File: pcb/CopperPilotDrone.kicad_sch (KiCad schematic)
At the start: 69 parts, among them IC1 MCP73833T-AMI/UN, J1 USB_C_Receptacle_USB2.0, J2 Conn_01x02_Female, J3 B2B-PH-SM4-TB(LF)(SN), J4 Conn_01x02_Female, J5 Conn_01x02_Female, J6 Conn_01x02_Female, SW1 PCM12SMTR, SW2 TS-1187A, SW3 TS-1187A, T1 SI2302DS-T1, T2 SI2302DS-T1, T3 SI2302DS-T1, T4 SI2302DS-T1, U2 AO3401, U3 AP2112K-3.3TRG1, U8 ESP32-S3-WROOM-1-N8R8, U9 MPU-6500

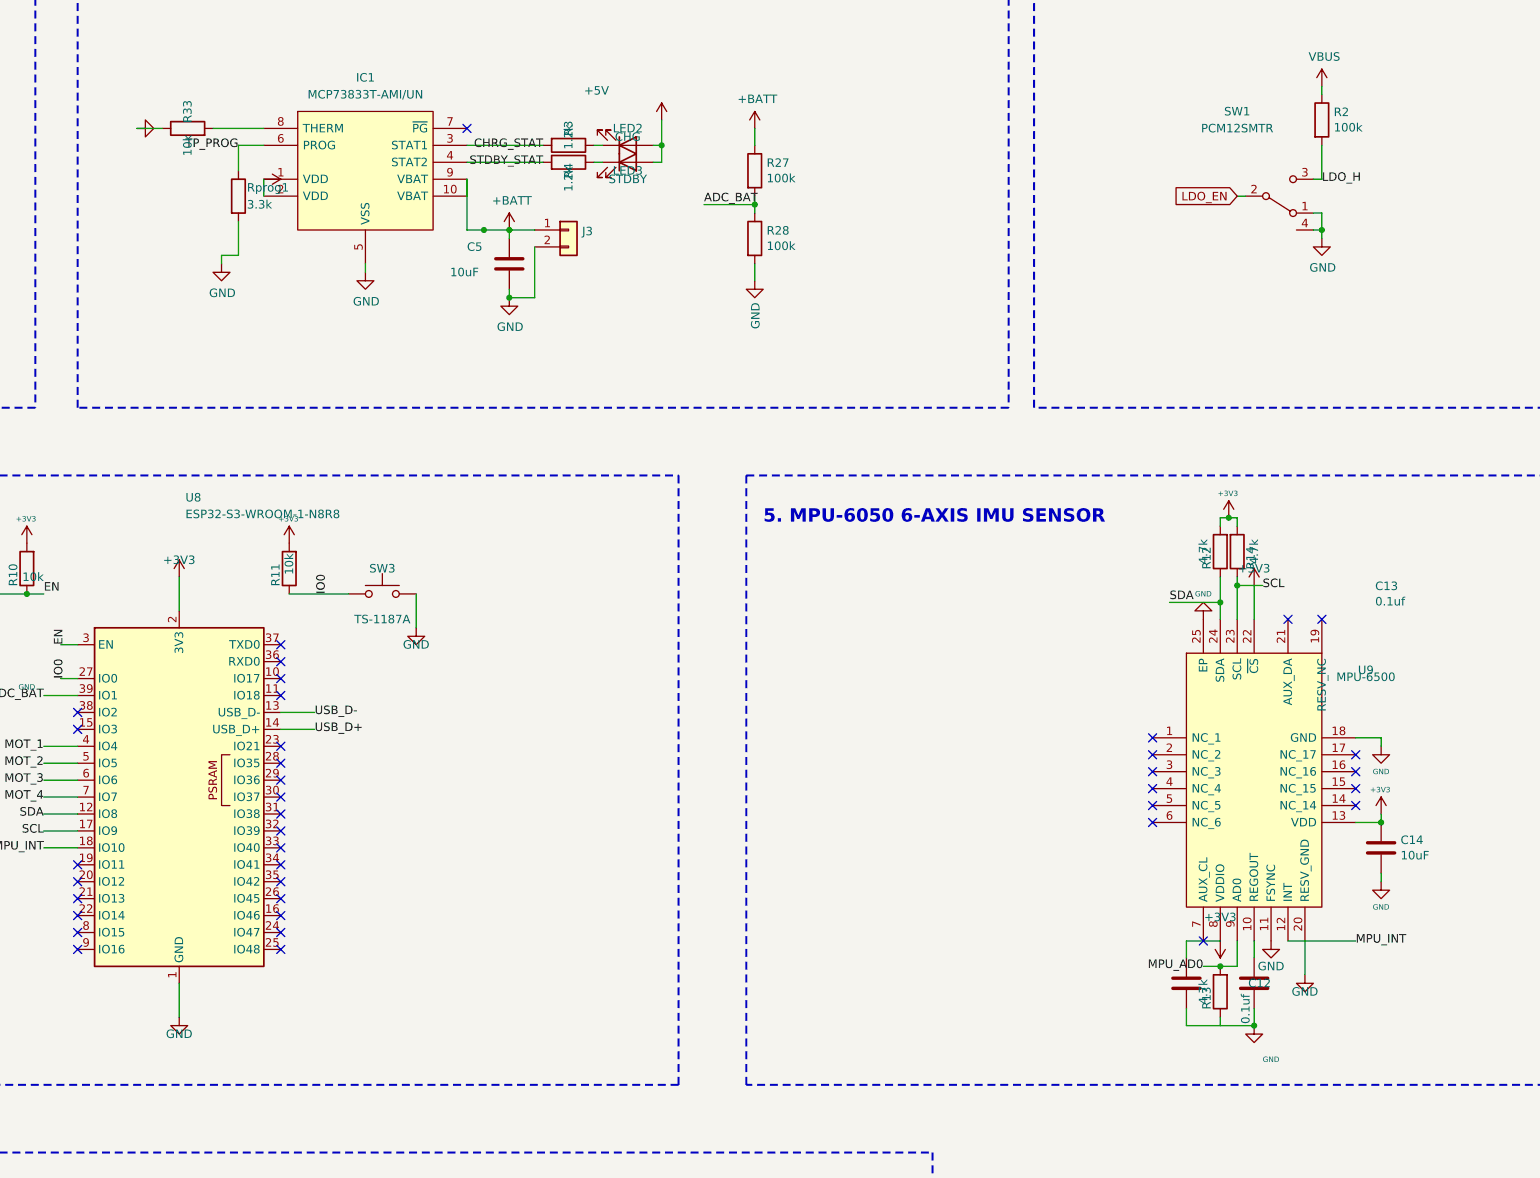
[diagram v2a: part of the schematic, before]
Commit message: fix(sch): complete GND symbol #PWR913 and pin ties on IC1/U9 for zero ERC
Verify 0 ERC violations across all severities via kicad-cli sch erc.

Co-Authored-By: CopperPilot <noreply@copperpilot.ai>
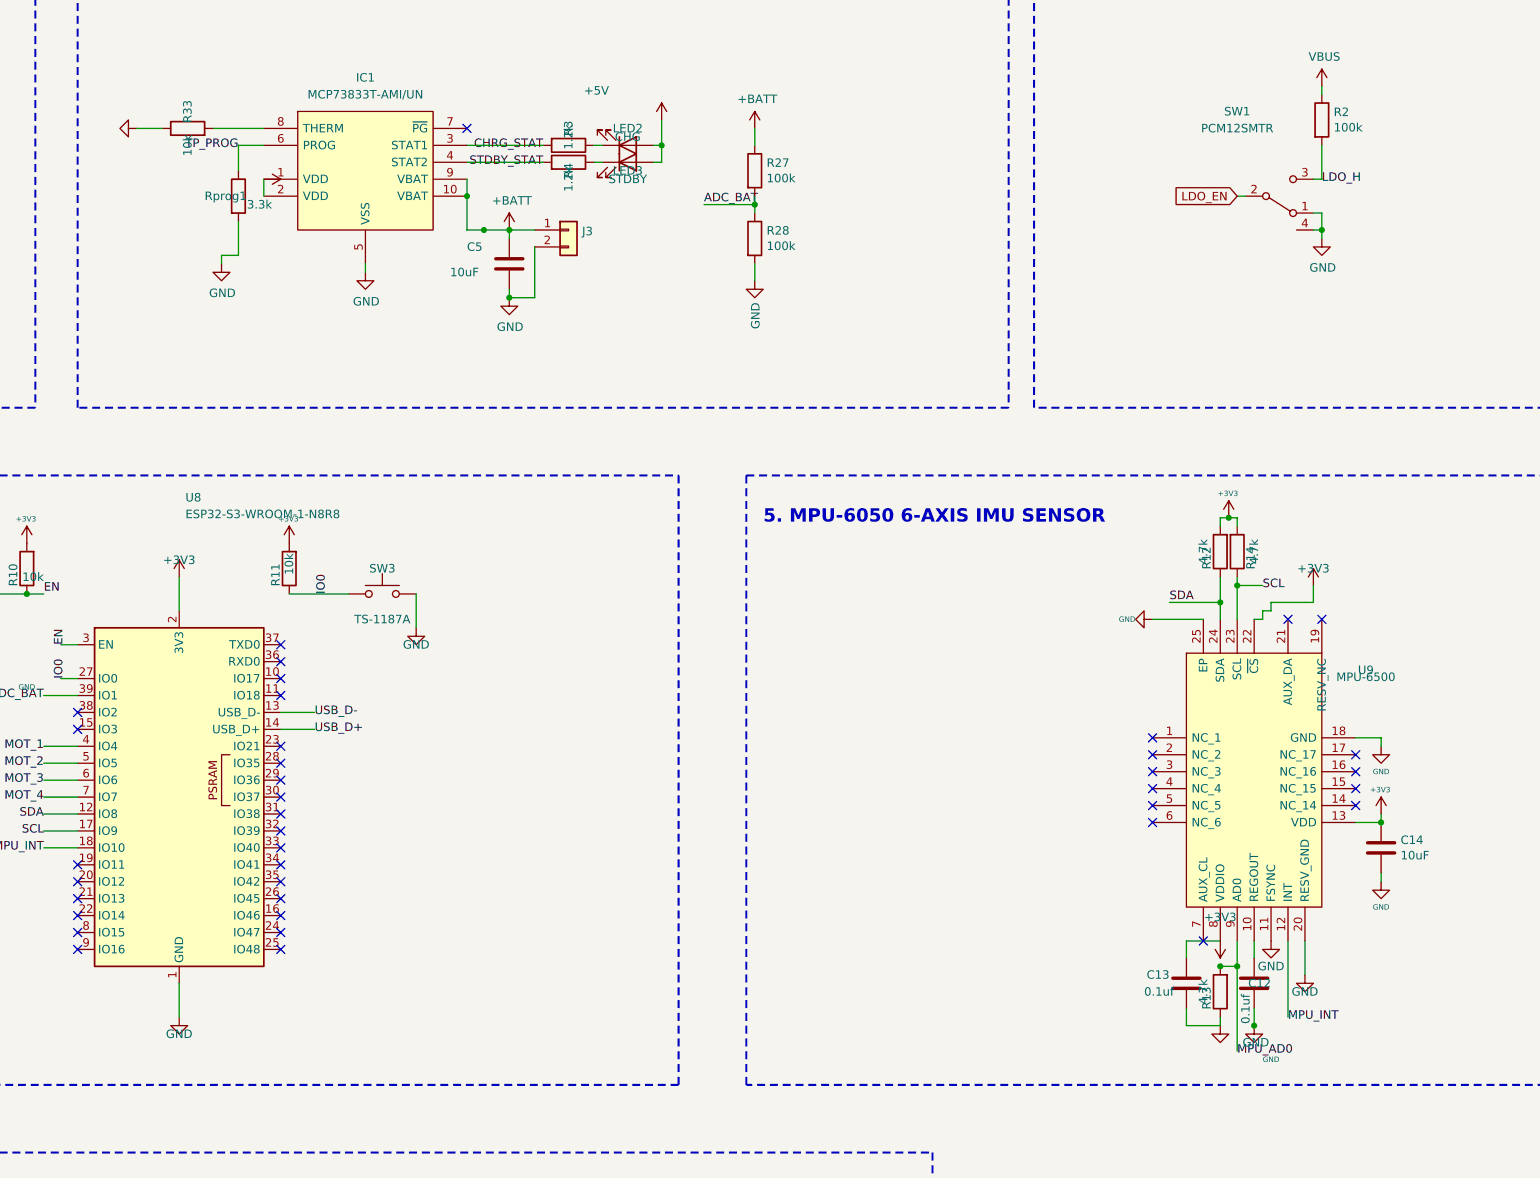
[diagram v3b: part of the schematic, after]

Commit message: fix(pcb): route MCP73833 charger, MPU-6500 IMU, and R33 pull-down with 0 DRC violations
Complete surgical layout redesign on PCB:
- Update IC1 footprint to MSOP-10 (Microchip MCP73833T-AMI/UN) and route +5V, +BATT, GND, /TP_PROG, /STDBY_STAT, and /CHRG_STAT
- Update U9 footprint to QFN-24 3x3mm (TDK InvenSense MPU-6500) and route I2C (SDA, SCL), INT, AD0, REGOUT, and power/GND
- Add R33 10k 0603 pull-down resistor on B.Cu for MCP73833 THERM pin
- Refill copper zones and verify with KiCad 10 DRC (0 violations, 0 unconnected items) and ERC (0 violations)

Co-Authored-By: CopperPilot <noreply@copperpilot.ai>
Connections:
- net CHRG_STAT: now also IC1.4 (STAT2), R4.2; no longer IC1.3 (STAT1), R3.2
- net STDBY_STAT: now also IC1.3 (STAT1), R3.2; no longer IC1.4 (STAT2), R4.2

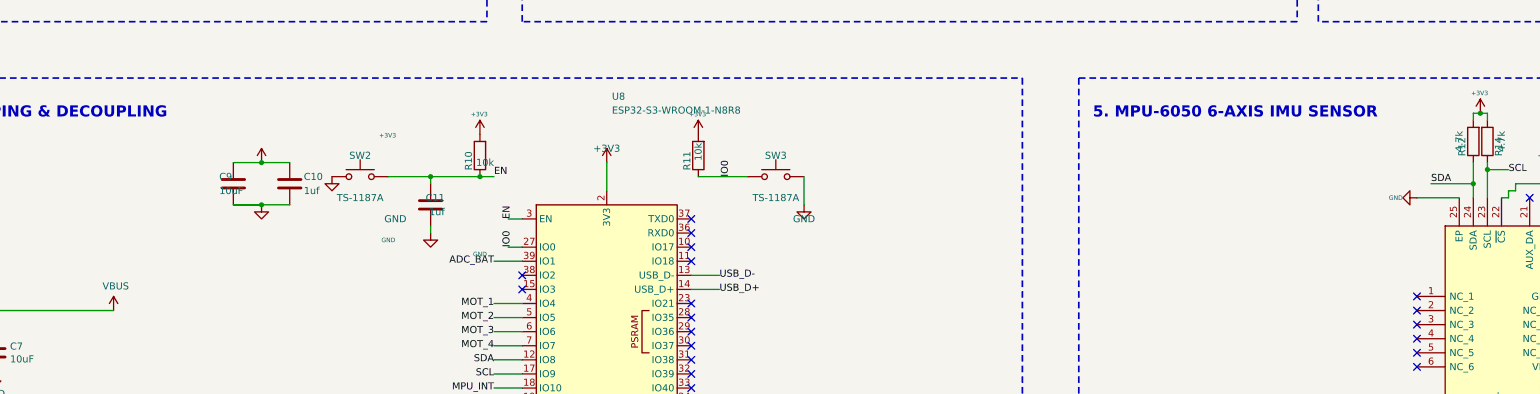
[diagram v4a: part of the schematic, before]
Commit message: fix(pcb,sch): resolve Issue #3 +BATT trunk, +5V charger decoupling, T4 flyback loop, and U8 keepout
- Rewire #PWR028 from VBUS to +5V so C6 (100 nF) and C7 (10 uF) decouple the +5V charger input rail (D1.2 / IC1 VDD) while VBUS retains C1 (10 uF)
- Widen J3.1 +BATT F.Cu exit to dual 1.27 mm paths and add 3x 0.8/0.4 mm stitching vias tying directly into the 1.524 mm B.Cu +BATT trunk
- Reposition D5 adjacent to T4 drain (2.15 mm direct path, down from 12.32 mm) and place C18/R32 with zero courtyard overlaps
- Add copperpour keepout behind U8 Pads 1 and 40 with dedicated inward GND ties and stitching vias
- Verified 0 ERC errors, 0 DRC errors, 0 unconnected nets, and 32/32 PCB pytest checks passing

Co-Authored-By: CopperPilot <noreply@copperpilot.ai>
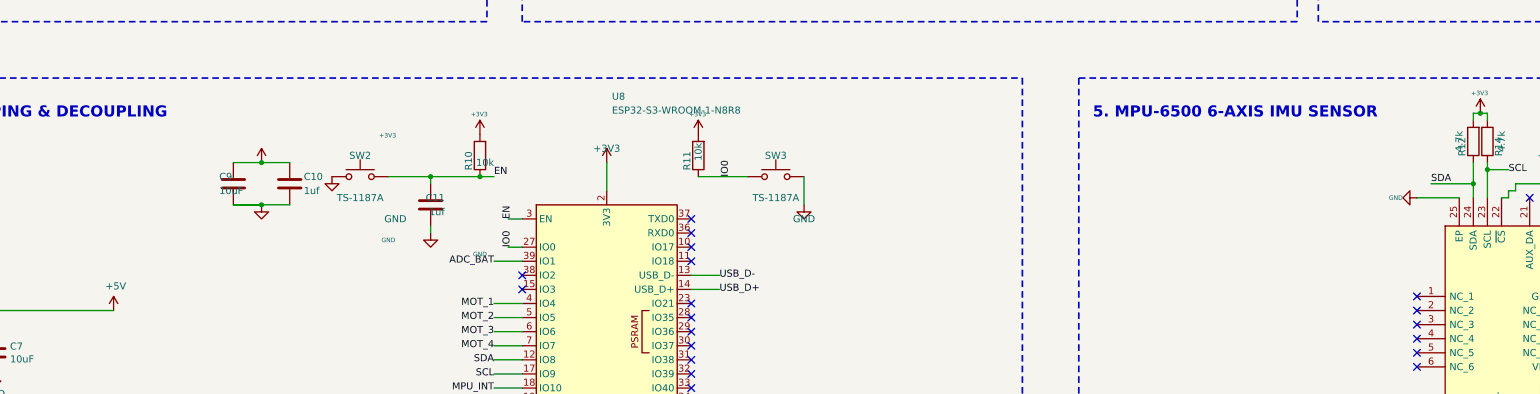
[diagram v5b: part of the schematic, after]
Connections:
- net +5V: now also C6.1, C7.1
- net VBUS: no longer C6.1, C7.1
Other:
- note added: "5. MPU-6500 6-AXIS IMU SENSOR"
- note removed: "5. MPU-6050 6-AXIS IMU SENSOR"
